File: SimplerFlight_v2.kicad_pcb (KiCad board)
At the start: 2 copper layers, 93.8 x 73.5 mm, 114 parts, among them J1 Battery 1, J10 Cam 3, J11 Servo, J12 Cam 2, J13 SWD Header, J14 DM3CS-SF, J2 Encoder, J7 Battery 2, J8 USB, J9 Cam 1, Q1 BSS816NWH6327XTSA1, Q2 NPN, Q3 BSS816NWH6327XTSA1, Q6 BSS816NWH6327XTSA1, SW1 Boot Switch, SW2 System Reset, U1 AMS1117-3.3, U2 STM32F401RETx, U3 BMP581, U4 BNO085, U5 TPS56A37RPAR, U6 TPS56A37RPAR, U7 MX25V4006EM1I-13G, Y2 Crystal

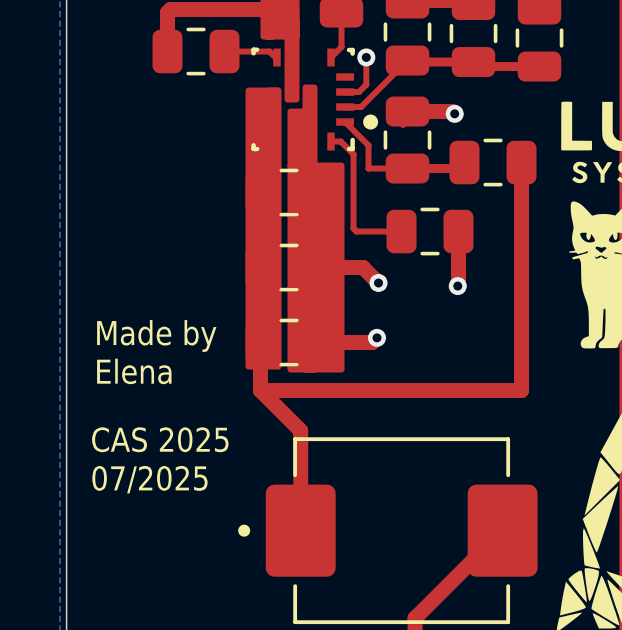
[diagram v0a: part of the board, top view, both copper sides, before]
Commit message: Adi made some fixes to schematic
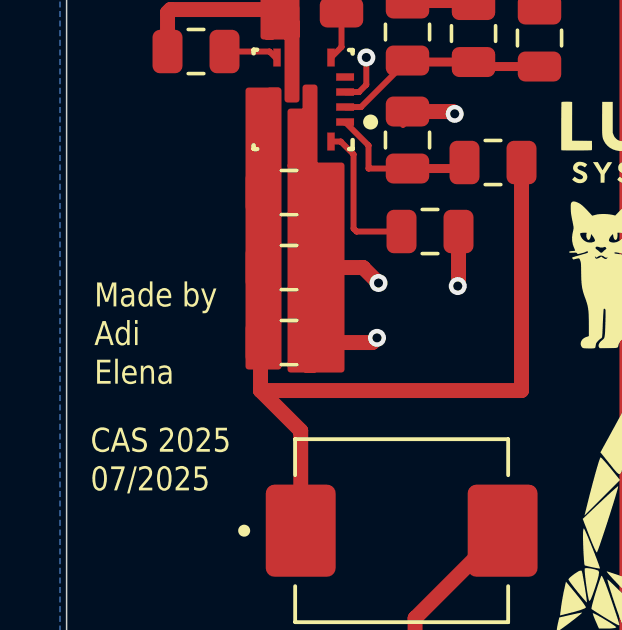
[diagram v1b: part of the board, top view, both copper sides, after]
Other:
- board text added: "Made by Adi Elena"
- board text removed: "Made by Elena"
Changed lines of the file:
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@@
 			(psa4output no)
 			(plot_black_and_white yes)
+			(plotinvisibletext no)
 			(sketchpadsonfab no)
 			(plotpadnumbers no)
@@
 		(layer "Edge.Cuts")
 	)
-	(gr_text "Made by\nElena"
+	(gr_text "Made by\nAdi\nElena"
 		(at 145.923 110.236 0)
 		(layer "F.SilkS")

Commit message: CLEAN ROUTES
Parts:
- removed C1: 10uF, Capacitor_SMD:C_0805_2012Metric
- removed C2, C20, C21, C22, C23, C24, C3, C4, C5, C6: 100nF, Capacitor_SMD:C_0805_2012Metric
- removed C25, C26: 15pF, Capacitor_SMD:C_0805_2012Metric
- removed C27: 100nF, Capacitor_SMD:C_0805_2012Metric_Pad1.18x1.45mm_HandSolder
- removed ENCA, ENCB, MISO, NRST, SCK, SWCLK, SWDIO: 5016, 5016:KEYSTONE_5016
- removed LS2: CBT-09427-SMT, CBT_09427_SMT_TR:CUI_CBT-09427-SMT
- removed MOSI : 5016, 5016:KEYSTONE_5016
- removed Q1, Q3, Q6: BSS816NWH6327XTSA1, BSS816NWH6327XTSA1:SOT65P210X100-3N
- removed Q2: NPN, FSB560A:SSOT3_3X1P5_ONS
- removed R13, R14: 2.2kR, Resistor_SMD:R_0805_2012Metric_Pad1.20x1.40mm_HandSolder
- removed R15: 10kR, Resistor_SMD:R_0805_2012Metric_Pad1.20x1.40mm_HandSolder
- removed R16, R17: 10k, Resistor_SMD:R_0805_2012Metric_Pad1.20x1.40mm_HandSolder
- removed R18, R20, R25, R26: 1kR, Resistor_SMD:R_0805_2012Metric_Pad1.20x1.40mm_HandSolder
- removed R19: 470, Resistor_SMD:R_0805_2012Metric_Pad1.20x1.40mm_HandSolder
- removed R2: 10k, Capacitor_SMD:C_0805_2012Metric
- removed R3, R4: 1k5, Capacitor_SMD:C_0805_2012Metric
- removed U2: STM32F401RETx, Package_QFP:LQFP-64_10x10mm_P0.5mm
- removed U3: BMP581, BMP581:QFN10_BMP581_BOS
- removed U4: BNO085, BNO085:IC_BNO085
- removed U7: MX25V4006EM1I-13G, MX25V4006EM1I-13G:SOP8_150_MAC
- removed Y2: Crystal, Crystal:Crystal_SMD_0603-2Pin_6.0x3.5mm_HandSoldering
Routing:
- net /Headers/+3V3: track 250.1 -> 0.19 mm
- net /Microcontroller/ENC_B: track 101.4 -> 0.00 mm, vias 2 -> 0
- net /Microcontroller/SPI1_MOSI: track 96.8 -> 0.00 mm, vias 10 -> 0
- net /Microcontroller/ENC_A: track 93.9 -> 0.00 mm, vias 2 -> 0
- net /Microcontroller/USART6_RX: track 89.6 -> 0.00 mm, vias 6 -> 0
- net /Microcontroller/SERVO_PWM: track 86.8 -> 0.00 mm, vias 12 -> 0
- net /Microcontroller/USART6_TX: track 86.3 -> 0.00 mm, vias 6 -> 0
- net /Microcontroller/SPI1_SCK: track 75.5 -> 0.00 mm, vias 8 -> 0
- net GND: track 117.9 -> 42.6 mm, vias 57 -> 24
- net /Peripherals/5V_CAM: track 74.8 -> 0.00 mm
- net /Microcontroller/SPI1_MISO: track 73.9 -> 0.00 mm, vias 10 -> 0
- net /Microcontroller/USART2_RX: track 72.2 -> 0.00 mm, vias 6 -> 0
- net /Microcontroller/SD_MEM_CS: track 68.5 -> 0.00 mm, vias 6 -> 0
- net /Microcontroller/USART2_TX: track 65.5 -> 0.00 mm, vias 4 -> 0
- net /Microcontroller/USART1_RX: track 64.6 -> 0.00 mm, vias 2 -> 0
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- removed copper zone on B.Cu, net GND
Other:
- copper layers 2 -> 4
- board text removed: "BARO"
- board text removed: "FLASH"
- board text removed: "IMU"

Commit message: sync
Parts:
- removed PWM: 5016, 5016:KEYSTONE_5016
- added C1: 10uF, Capacitor_SMD:C_0805_2012Metric, F.Cu at (103.3, 104.9)
- added C2: 100nF, Capacitor_SMD:C_0805_2012Metric, F.Cu at (103.3, 107.9)
- added C20: 100nF, Capacitor_SMD:C_0805_2012Metric, F.Cu at (119.8, 90.4)
- added C21: 100nF, Capacitor_SMD:C_0805_2012Metric, F.Cu at (119.8, 93.4)
- added C22: 100nF, Capacitor_SMD:C_0805_2012Metric, F.Cu at (119.8, 96.4)
- added C23: 100nF, Capacitor_SMD:C_0805_2012Metric, F.Cu at (119.8, 99.4)
- added C24: 100nF, Capacitor_SMD:C_0805_2012Metric, F.Cu at (119.8, 102.4)
- added C25: 15pF, Capacitor_SMD:C_0805_2012Metric, F.Cu at (119.8, 105.5)
- added C26: 15pF, Capacitor_SMD:C_0805_2012Metric, F.Cu at (119.8, 108.5)
- added C27: 100nF, Capacitor_SMD:C_0805_2012Metric_Pad1.18x1.45mm_HandSolder, F.Cu at (129.0, 122.6)
- added C28: 100nF, Capacitor_SMD:C_0805_2012Metric, F.Cu at (128.8, 125.6)
- added C3: 100nF, Capacitor_SMD:C_0805_2012Metric, F.Cu at (103.3, 110.9)
- added C4: 100nF, Capacitor_SMD:C_0805_2012Metric, F.Cu at (107.8, 104.9)
- added C5: 100nF, Capacitor_SMD:C_0805_2012Metric, F.Cu at (107.8, 107.9)
- added C6: 100nF, Capacitor_SMD:C_0805_2012Metric, F.Cu at (107.8, 110.9)
- added LS2: CBT-09427-SMT, CBT_09427_SMT_TR:CUI_CBT-09427-SMT, F.Cu at (85.8, 124.5)
- added Q2: NPN, FSB560A:SSOT3_3X1P5_ONS, F.Cu at (96.8, 102.4)
- added Q5: BSS816NWH6327XTSA1, BSS816NWH6327XTSA1:SOT65P210X100-3N, F.Cu at (96.8, 90.8)
- added Q6: BSS816NWH6327XTSA1, BSS816NWH6327XTSA1:SOT65P210X100-3N, F.Cu at (96.8, 94.5)
- added Q7: BSS816NWH6327XTSA1, BSS816NWH6327XTSA1:SOT65P210X100-3N, F.Cu at (96.8, 98.3)
- added R13: 2.2kR, Resistor_SMD:R_0805_2012Metric_Pad1.20x1.40mm_HandSolder, F.Cu at (124.4, 90.4)
- added R14: 2.2kR, Resistor_SMD:R_0805_2012Metric_Pad1.20x1.40mm_HandSolder, F.Cu at (124.4, 93.3)
- added R15: 10kR, Resistor_SMD:R_0805_2012Metric_Pad1.20x1.40mm_HandSolder, F.Cu at (124.4, 96.3)
- added R16: 10k, Resistor_SMD:R_0805_2012Metric_Pad1.20x1.40mm_HandSolder, F.Cu at (124.2, 122.5)
- added R17: 10k, Resistor_SMD:R_0805_2012Metric_Pad1.20x1.40mm_HandSolder, F.Cu at (124.2, 125.5)
- added R18: 1kR, Resistor_SMD:R_0805_2012Metric_Pad1.20x1.40mm_HandSolder, F.Cu at (92.2, 90.4)
- added R19: 470, Resistor_SMD:R_0805_2012Metric_Pad1.20x1.40mm_HandSolder, F.Cu at (92.2, 93.3)
- added R2: 10k, Capacitor_SMD:C_0805_2012Metric, F.Cu at (112.2, 104.9)
- added R20: 100R, Resistor_SMD:R_0805_2012Metric_Pad1.20x1.40mm_HandSolder, F.Cu at (92.2, 96.3)
- added R25: 100R, Resistor_SMD:R_0805_2012Metric_Pad1.20x1.40mm_HandSolder, F.Cu at (92.2, 99.2)
- added R26: 100R, Resistor_SMD:R_0805_2012Metric_Pad1.20x1.40mm_HandSolder, F.Cu at (92.2, 102.2)
- added R3: 1k5, Capacitor_SMD:C_0805_2012Metric, F.Cu at (112.2, 107.9)
- added R32: 10k, Resistor_SMD:R_0805_2012Metric_Pad1.20x1.40mm_HandSolder, F.Cu at (124.4, 99.2)
- added R33: 10kR, Resistor_SMD:R_0805_2012Metric_Pad1.20x1.40mm_HandSolder, F.Cu at (92.2, 105.1)
- added R34: 10kR, Resistor_SMD:R_0805_2012Metric_Pad1.20x1.40mm_HandSolder, F.Cu at (92.2, 108.1)
- added R35: 10kR, Resistor_SMD:R_0805_2012Metric_Pad1.20x1.40mm_HandSolder, F.Cu at (92.2, 111.0)
- added R4: 1k5, Capacitor_SMD:C_0805_2012Metric, F.Cu at (112.2, 110.9)
- added TP1: 5016, 5016:KEYSTONE_5016, F.Cu at (104.2, 116.9)
- added TP11: 5016, 5016:KEYSTONE_5016, F.Cu at (116.7, 116.9)
- added TP12: 5016, 5016:KEYSTONE_5016, F.Cu at (116.7, 121.9)
- added TP13: 5016, 5016:KEYSTONE_5016, F.Cu at (116.7, 126.8)
- added TP2: 5016, 5016:KEYSTONE_5016, F.Cu at (104.2, 121.9)
- added TP3: 5016, 5016:KEYSTONE_5016, F.Cu at (104.2, 126.8)
- added TP4: 5016, 5016:KEYSTONE_5016, F.Cu at (104.2, 131.8)
- added TP5: 5016, 5016:KEYSTONE_5016, F.Cu at (110.5, 116.9)
- added TP6: 5016, 5016:KEYSTONE_5016, F.Cu at (110.5, 121.9)
- added TP7: 5016, 5016:KEYSTONE_5016, F.Cu at (110.5, 126.8)
- added TP8: 5016, 5016:KEYSTONE_5016, F.Cu at (110.5, 131.8)
- added U2: STM32F401RETx, Package_QFP:LQFP-64_10x10mm_P0.5mm, F.Cu at (108.3, 96.1)
- added U3: BMP581, BMP581:QFN10_BMP581_BOS, F.Cu at (128.7, 96.5)
- added U4: BNO085, BNO085:IC_BNO085, F.Cu at (130.1, 91.9)
- added U7: MX25V4006EM1I-13G, MX25V4006EM1I-13G:SOP8_150_MAC, F.Cu at (126.2, 117.7)
- added Y2: Crystal, Crystal:Crystal_SMD_0603-2Pin_6.0x3.5mm_HandSoldering, F.Cu at (127.4, 103.2)
- J10: value Cam 3 -> Cam 1
- J12: value Cam 2 -> Cam 1
- moved G*** 60.3 mm to (117.6, 142.8)
- moved G*** 60.3 mm to (116.7, 153.8)
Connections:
- J10 pad 1: /Peripherals/CAM_3_VO -> /Peripherals/5V_CAM
- J10 pad 2: GND -> Net-(Q6-D)
- J10 pad 3: /Microcontroller/USART6_RX -> /Microcontroller/USART2_RX
- J10 pad 4: /Microcontroller/USART6_TX -> /Microcontroller/USART2_TX
- J10 pad 5: GND -> unconnected-(J10-Pad5)
- J12 pad 1: /Peripherals/CAM_2_VO -> /Peripherals/5V_CAM
- J12 pad 2: GND -> Net-(Q7-D)
- J12 pad 3: /Microcontroller/USART2_RX -> /Microcontroller/USART6_RX
- J12 pad 4: /Microcontroller/USART2_TX -> /Microcontroller/USART6_TX
- J12 pad 5: GND -> unconnected-(J12-Pad5)
- J9 pad 1: /Peripherals/CAM_1_VO -> /Peripherals/5V_CAM
- J9 pad 2: GND -> Net-(Q5-D)
- J9 pad 5: GND -> unconnected-(J9-Pad5)
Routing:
- net /Power/VIN_CAM: track 35.0 -> 25.8 mm
- net /Peripherals/5V_SERVO: track 8.73 -> 0.40 mm

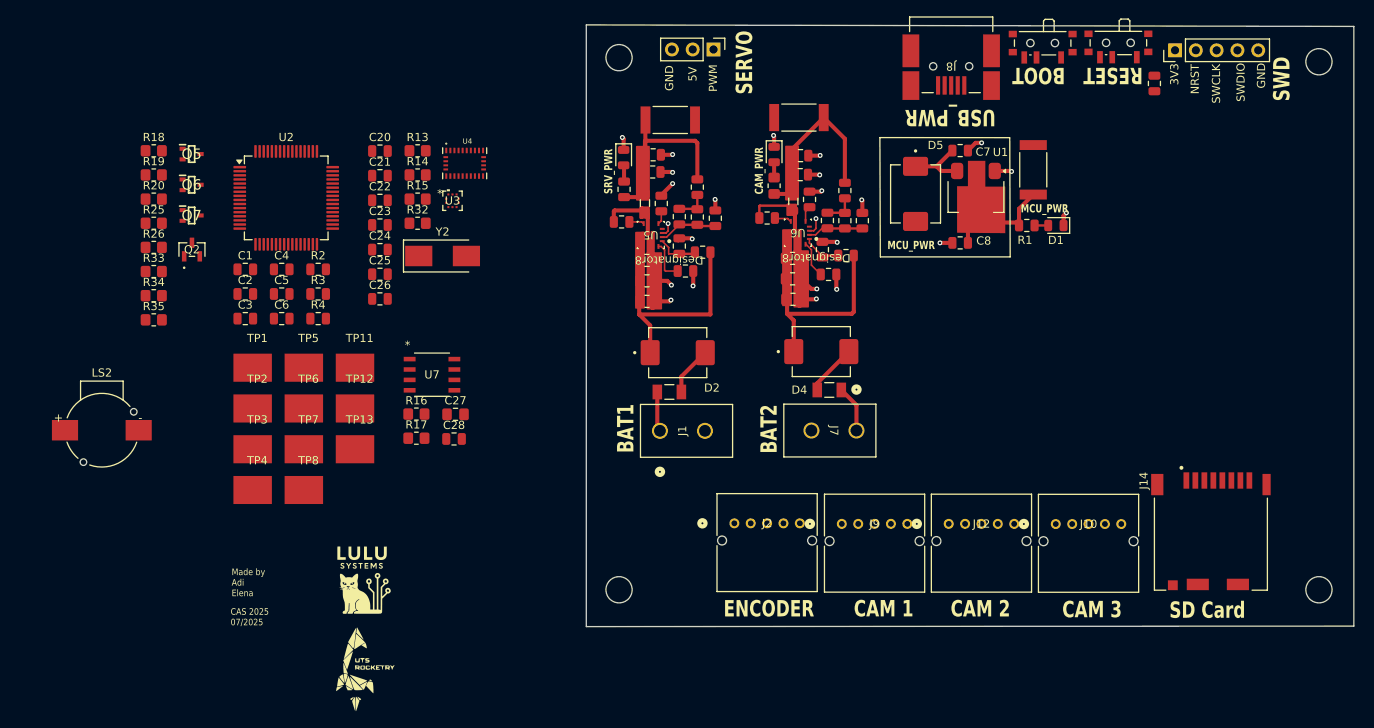
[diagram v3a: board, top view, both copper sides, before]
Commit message: Update capacitor model for Cin for servo motor power supply
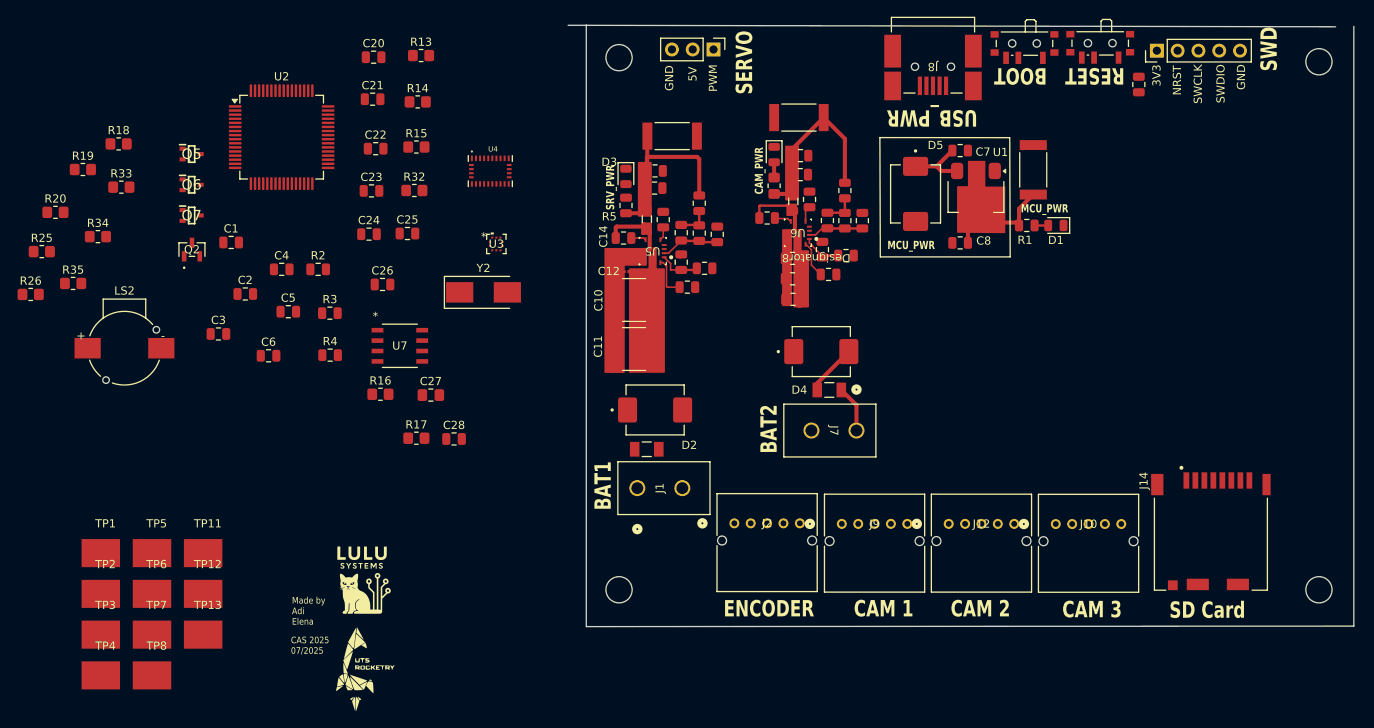
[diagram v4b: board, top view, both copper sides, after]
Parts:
- C10, C11: footprint Capacitor_SMD:C_0805_2012Metric -> Capacitor_SMD:C_2220_5750Metric
- C12: footprint Capacitor_SMD:C_0805_2012Metric -> Capacitor_SMD:C_0201_0603Metric
- moved TP13 29.3 mm to (98.2, 149.5)
- moved TP3 29.3 mm to (85.7, 149.5)
- moved TP7 29.3 mm to (91.9, 149.5)
- moved TP1 29.3 mm to (85.7, 139.5)
- moved TP11 29.3 mm to (98.2, 139.5)
- moved TP12 29.3 mm to (98.2, 144.5)
- moved TP2 29.3 mm to (85.7, 144.5)
- moved TP4 29.3 mm to (85.7, 154.5)
- moved TP5 29.3 mm to (91.9, 139.5)
- moved TP6 29.3 mm to (91.9, 144.5)
- moved TP8 29.3 mm to (91.9, 154.5)
- moved R26 16.1 mm to (77.1, 107.9)
- moved R25 14.1 mm to (78.5, 102.7)
- moved R20 12.1 mm to (80.2, 97.9)
- moved R13 11.6 mm to (124.8, 78.7)
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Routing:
- net GND: track 42.6 -> 0.22 mm, vias 24 -> 0
- net /Power/VIN_CAM: track 25.8 -> 0.06 mm
- net /Power/VIN_SERVO: track 23.1 -> 0.00 mm
- net /Power/BAT_1: track 6.01 -> 0.00 mm
- net Net-(F1-Pad1): track 4.88 -> 0.45 mm
- net Net-(D3-A): track 2.01 -> 0.00 mm
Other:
- board size 93.8 x 73.5 mm -> 96 x 73.5 mm

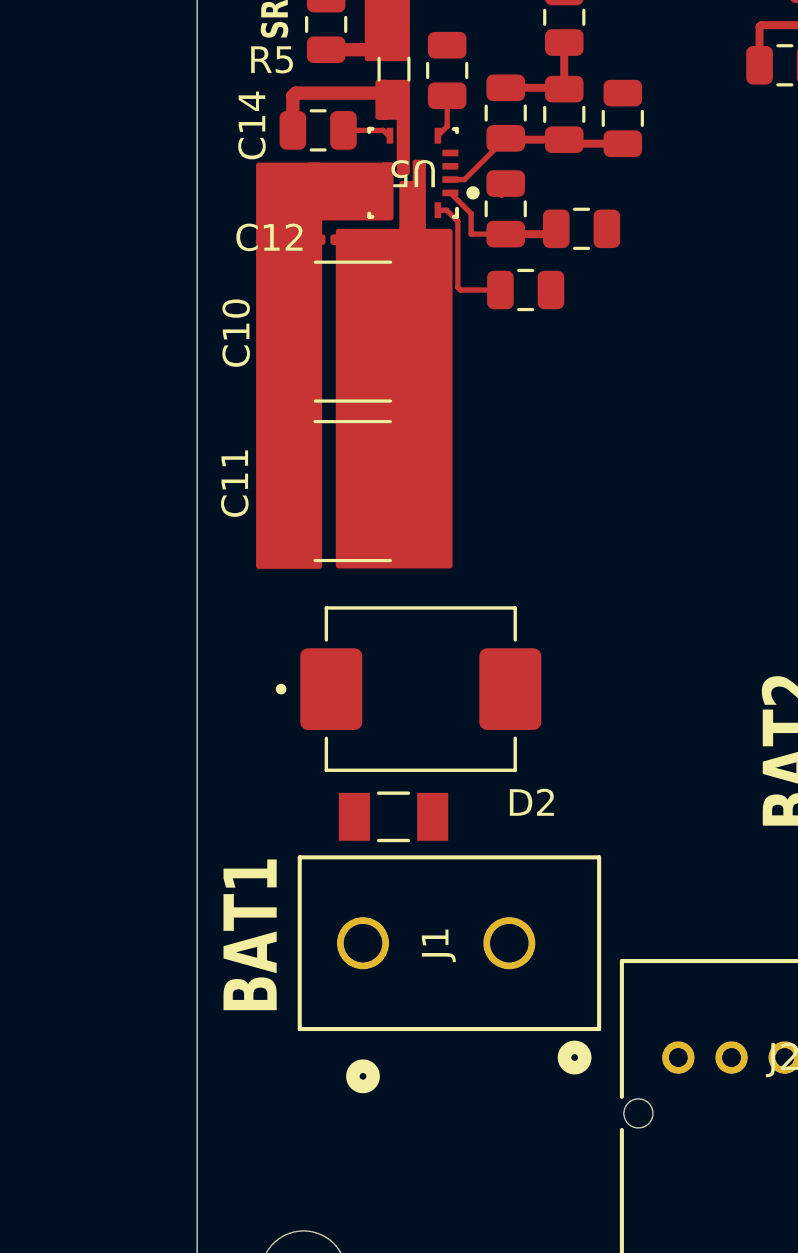
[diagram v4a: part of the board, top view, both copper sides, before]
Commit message: Update capacitor model for Cin for servo motor power supply
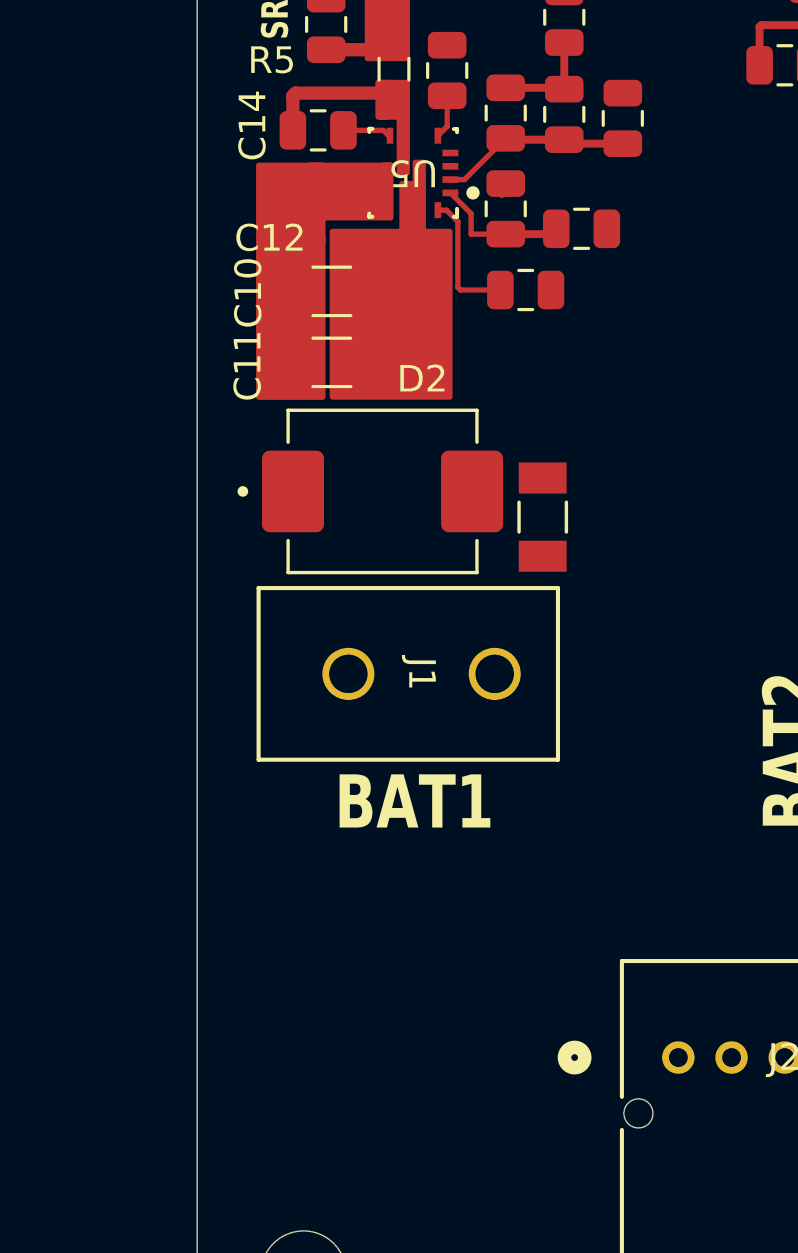
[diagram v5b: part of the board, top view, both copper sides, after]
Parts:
- C10, C11: footprint Capacitor_SMD:C_2220_5750Metric -> Capacitor_SMD:C_1206_3216Metric
- moved F1 12.6 mm to (158.0, 115.6), turned to 90 degrees
- moved J1 11.3 mm to (156.2, 121.5), turned to -90 degrees
- moved D2 7.57 mm to (152.0, 114.6)
- moved C11 4.90 mm to (150.1, 109.8)
- moved C10 1.71 mm to (150.1, 107.1)
